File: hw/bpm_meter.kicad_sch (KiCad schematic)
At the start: 72 parts, among them J1 Conn_01x03_Pin, Q1 AO3400A, Q10 DMN2004VK, Q11 DMN2004VK, Q12 DMN2004VK, Q13 DMN2004VK, Q2 DMN2004VK, Q3 DMN2004VK, Q4 DMN2004VK, Q5 DMN2004VK, Q6 DMN2004VK, Q7 DMN2004VK, Q8 DMN2004VK, Q9 DMN2004VK, U1 SLS0391FR1A1GD, U2 AOZ1282CI, U3 H11L1, U4 SLS0391FR1A1GD, U5 SLS0391FR1A1GD

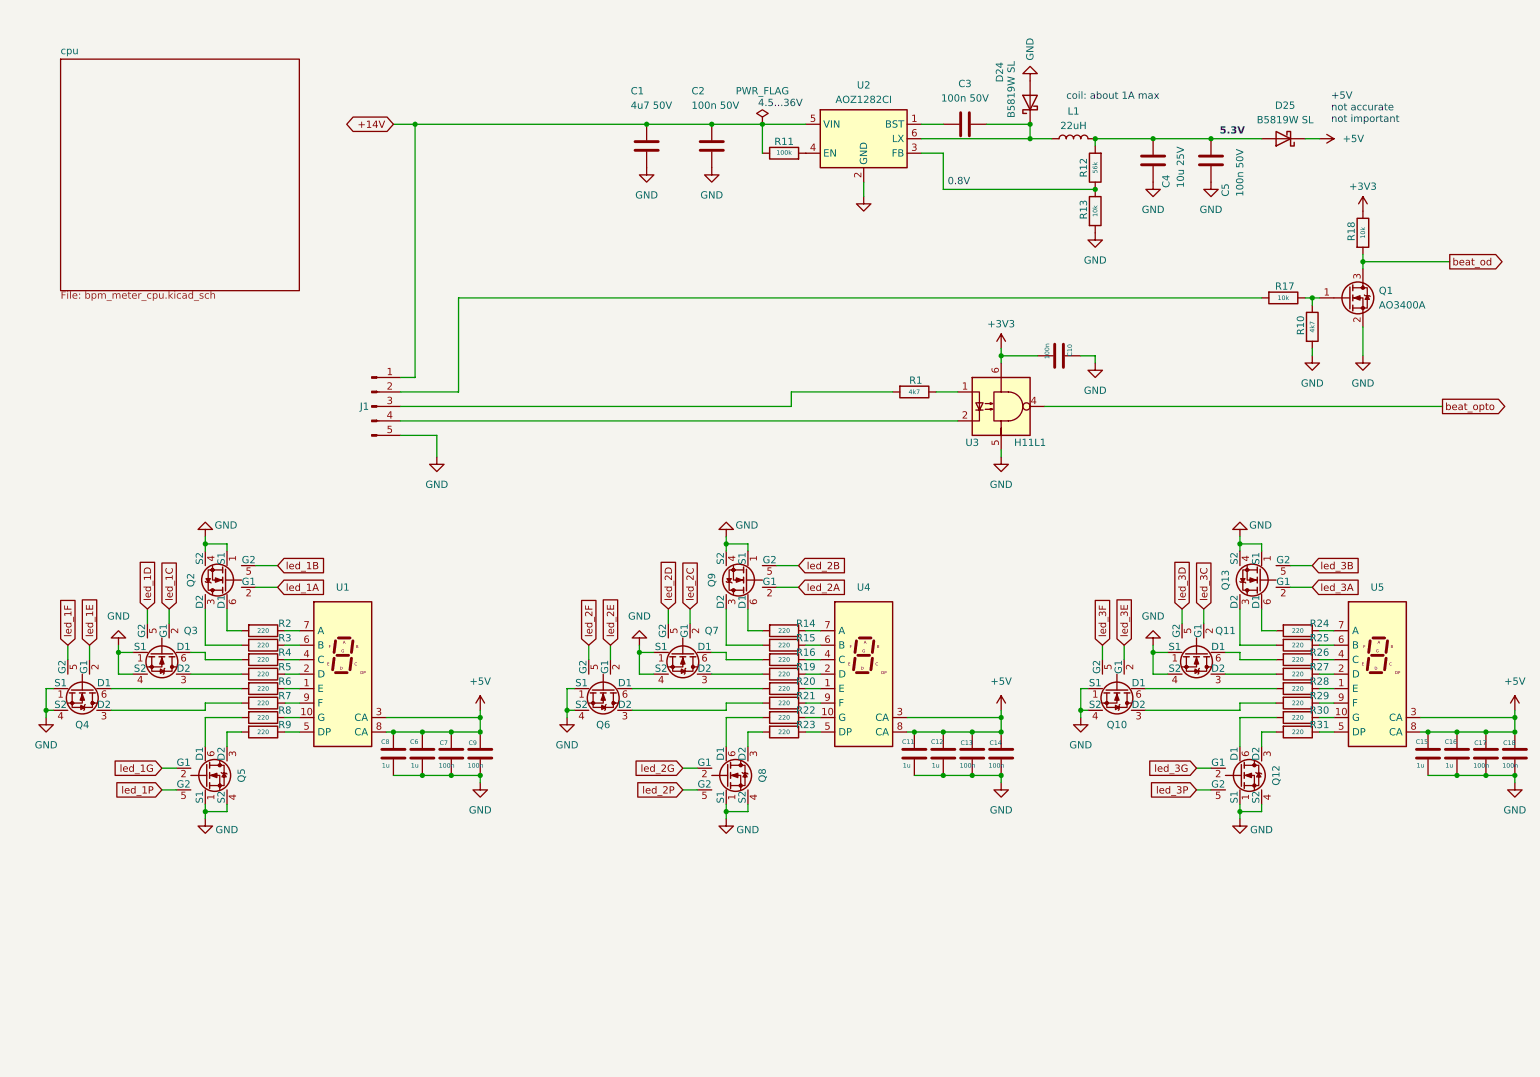
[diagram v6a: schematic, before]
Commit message: Now using LP5030 LED driver
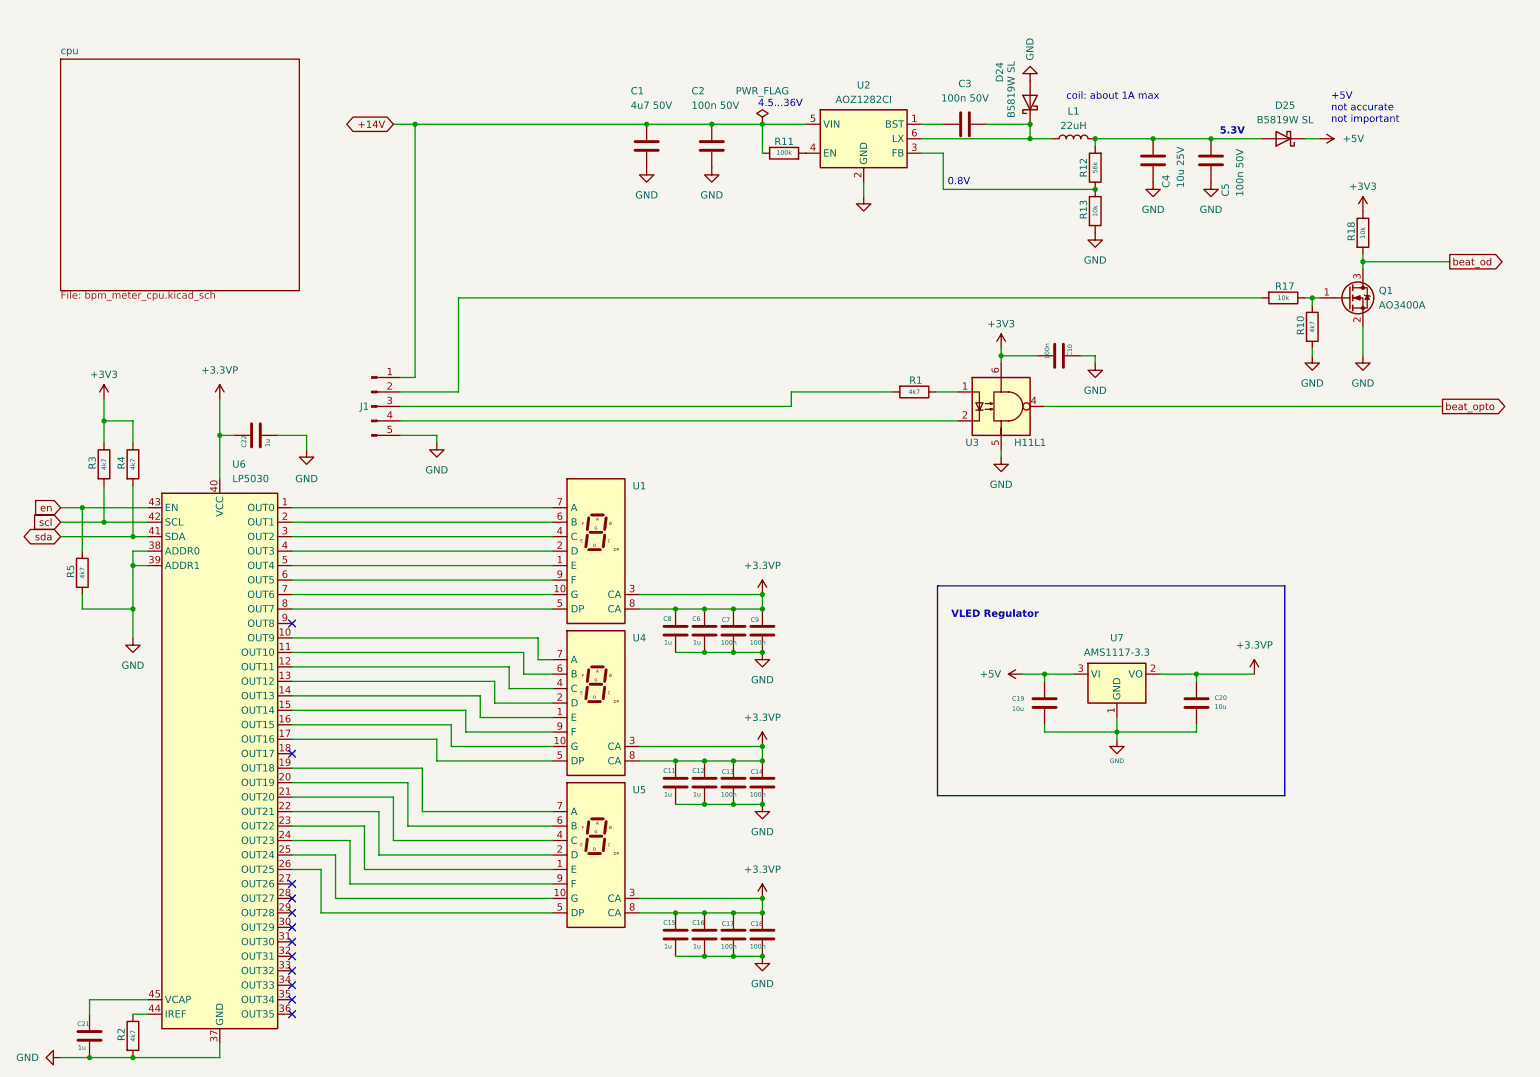
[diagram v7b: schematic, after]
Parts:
- removed Q10, Q11, Q12, Q13, Q2, Q3, Q4, Q5, Q6, Q7, Q8, Q9: DMN2004VK, Package_TO_SOT_SMD:SOT-563, symbol 00_project_library:DMN60H080DS
- removed R14, R15, R16, R19, R20, R21, R22, R23, R24, R25, R26, R27, R28, R29, R30, R31, R6, R7, R8, R9: 220, Resistor_SMD:R_0402_1005Metric_Pad0.72x0.64mm_HandSolder, symbol Device:R
- added C19, C20: 10u, Capacitor_SMD:C_0603_1608Metric, symbol 00_project_library:C
- added C21, C22: 1u, Capacitor_SMD:C_0402_1005Metric, symbol 00_project_library:C
- added U6: LP5030, Package_DFN_QFN:VQFN-46-1EP_5x6mm_P0.4mm_EP2.8x3.8mm, symbol Driver_LED:LP5036
- added U7: AMS1117-3.3, 00_project_library:SOT-223-3_TabPin2, symbol 00_project_library:AMS1117-3.3
- J1: value Conn_01x03_Pin -> Conn_01x05_Pin
- R2, R3, R4, R5: value 220 -> 4k7; JLC C25091 -> (none)
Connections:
- net +3V3: now also R3.1, R4.1
- net +5V: now also C19.1, U7.3 (VI); no longer C11.1, C12.1, C13.1, C14.1, C15.1, C16.1, C17.1, C18.1, C6.1, C7.1, C8.1, C9.1, U1.3 (CA), U1.8 (CA), U4.3 (CA), U4.8 (CA), U5.3 (CA), U5.8 (CA)
- net GND: now also R2.2, R5.2, C19.2, C20.2, C21.2, C22.2, U6.37 (GND), U6.38 (ADDR0), U6.39 (ADDR1), U6.46 (GND), U6.47 (GND), U7.1 (GND)
- net scl: now reaches R3.2
- net scl: now also U6.42 (SCL)
- net at U1.7 (A): now also U6.1 (OUT0); no longer R2.1
- net at U4.4 (C): now also U6.12 (OUT11)
- net at U4.9 (F): now also U6.15 (OUT14)
- net at U1.9 (F): now also U6.6 (OUT5)
- net at U5.7 (A): now also U6.19 (OUT18)
- net at U5.10 (G): now also U6.25 (OUT24)
- net at U5.1 (E): now also U6.23 (OUT22)
- net at U5.2 (D): now also U6.22 (OUT21)
- net at U5.4 (C): now also U6.21 (OUT20)
- net at U5.5 (DP): now also U6.26 (OUT25)
- net at U5.6 (B): now also U6.20 (OUT19)
- net at U5.9 (F): now also U6.24 (OUT23)
- net at U1.4 (C): now also U6.3 (OUT2); no longer R4.1
- net sda: now reaches R4.2
- net sda: now also U6.41 (SDA)
- net at U4.7 (A): now also U6.10 (OUT9)
- net at U1.1 (E): now also U6.5 (OUT4)
- net at U1.10 (G): now also U6.7 (OUT6)
- net at U1.2 (D): now also U6.4 (OUT3); no longer R5.1
- net at U1.5 (DP): now also U6.8 (OUT7)
- net at U1.6 (B): now also U6.2 (OUT1); no longer R3.1
- net at U4.2 (D): now also U6.13 (OUT12)
- net at U4.1 (E): now also U6.14 (OUT13)
- net at U4.6 (B): now also U6.11 (OUT10)
- net at U4.10 (G): now also U6.16 (OUT15)
- net at U4.5 (DP): now also U6.17 (OUT16)
- new net: R2.1, U6.44 (IREF)
- new net: C21.1, U6.45 (VCAP)
- new net +3.3VP: C11.1, C12.1, C13.1, C14.1, C15.1, C16.1, C17.1, C18.1, C20.1, C22.1, C6.1, C7.1, C8.1, C9.1, U1.3 (CA), U1.8 (CA), U4.3 (CA), U4.8 (CA), U5.3 (CA), U5.8 (CA), U6.40 (VCC), U7.2 (VO)
- new net en: R5.1, U6.43 (EN)
- no-connect marks 0 -> 12
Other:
- note added: "VLED Regulator"
- moved on the sheet: C11, C12, C13, C14, C15, C16, C17, C18, C6, C7, C8, C9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

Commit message: Changed LED driver to ISSI IS31FL3236A
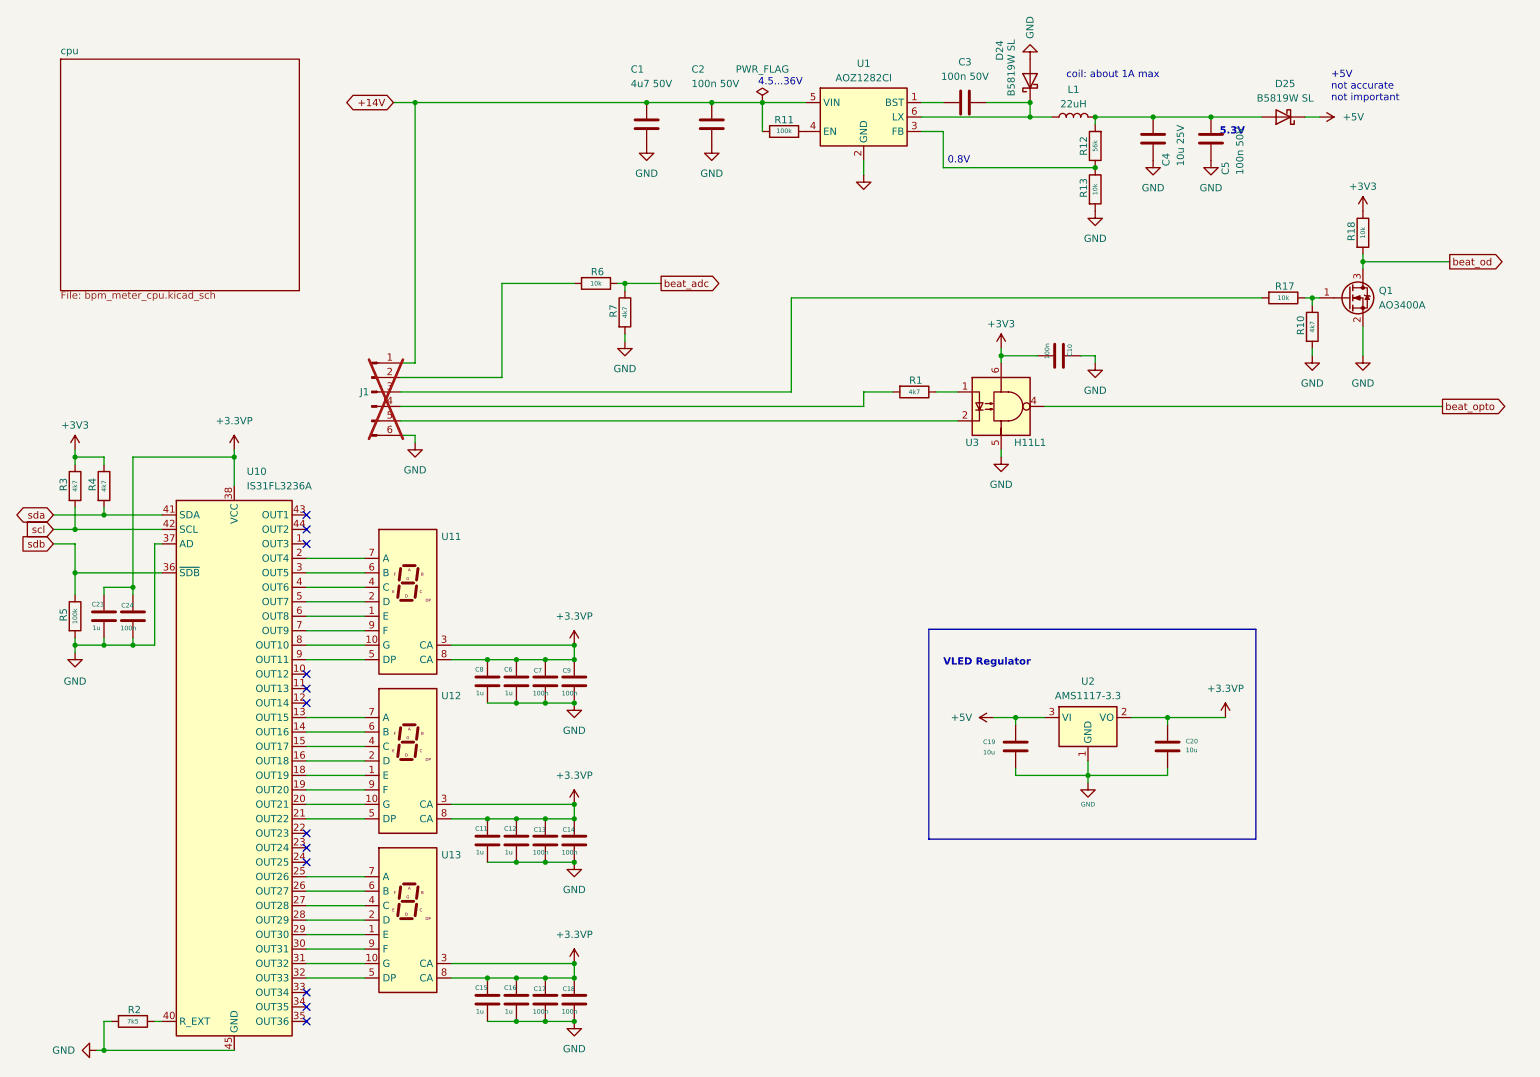
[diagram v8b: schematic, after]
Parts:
- removed C21, C22: 1u, Capacitor_SMD:C_0402_1005Metric, symbol 00_project_library:C
- removed U6: LP5030, Package_DFN_QFN:VQFN-46-1EP_5x6mm_P0.4mm_EP2.8x3.8mm, symbol Driver_LED:LP5036
- added C23: 1u, Capacitor_SMD:C_0402_1005Metric_Pad0.74x0.62mm_HandSolder, symbol 00_project_library:C
- added C24: 100n, Capacitor_SMD:C_0402_1005Metric_Pad0.74x0.62mm_HandSolder, symbol 00_project_library:C
- added R6: 10k, Resistor_SMD:R_0402_1005Metric_Pad0.72x0.64mm_HandSolder, symbol Device:R
- added R7: 4k7, Resistor_SMD:R_0402_1005Metric_Pad0.72x0.64mm_HandSolder, symbol Device:R
- added U10: IS31FL3236A, 00_project_library:QFN-44-5x5mm_P0.4mm, symbol 00_project_library:IS31FL3236A
- C10, C13, C14, C17, C18, C7, C9: footprint Capacitor_SMD:C_0402_1005Metric -> Capacitor_SMD:C_0402_1005Metric_Pad0.74x0.62mm_HandSolder; JLC C307331 -> (none)
- C11, C12, C15, C16, C6, C8: footprint Capacitor_SMD:C_0402_1005Metric -> Capacitor_SMD:C_0402_1005Metric_Pad0.74x0.62mm_HandSolder; JLC C52923 -> (none)
- J1: value Conn_01x05_Pin -> Conn_01x06_Pin; footprint Connector_PinHeader_2.54mm:PinHeader_1x05_P2.54mm_Vertical -> Connector_PinHeader_2.54mm:PinHeader_1x06_P2.54mm_Vertical; symbol Connector:Conn_01x05_Pin -> Connector:Conn_01x06_Pin; now not fitted
- R2: value 4k7 -> 7k5
- R5: value 4k7 -> 100k
- renumbered U2 to U1, U1 to U11, U4 to U12, U5 to U13, U7 to U2
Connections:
- net +3.3VP: now also C23.1, C24.1, U10.38 (VCC)
- net GND: now also J1.6 (Pin_6), C23.2, C24.2, R7.2, U10.17 (GND), U10.37 (AD), U10.39 (GND), U10.45 (GND); no longer J1.5 (Pin_5)
- net scl: now also U10.42 (SCL)
- net sda: now also U10.41 (SDA)
- net at U11.7 (A): now also U10.2 (OUT4)
- net at U12.7 (A): now also U10.13 (OUT15)
- net at U12.6 (B): now also U10.14 (OUT16)
- net at U12.4 (C): now also U10.15 (OUT17)
- net at U12.2 (D): now also U10.16 (OUT18)
- net at U12.1 (E): now also U10.18 (OUT19)
- net at U12.9 (F): now also U10.19 (OUT20)
- net at U12.10 (G): now also U10.20 (OUT21)
- net at U12.5 (DP): now also U10.21 (OUT22)
- net at U13.7 (A): now also U10.25 (OUT26)
- net at U11.6 (B): now also U10.3 (OUT5)
- net at U13.6 (B): now also U10.26 (OUT27)
- net at U13.4 (C): now also U10.27 (OUT28)
- net at U13.2 (D): now also U10.28 (OUT29)
- net at U13.1 (E): now also U10.29 (OUT30)
- net at U13.9 (F): now also U10.30 (OUT31)
- net at U13.10 (G): now also U10.31 (OUT32)
- net at U13.5 (DP): now also U10.32 (OUT33)
- net at U11.4 (C): now also U10.4 (OUT6)
- net at U11.2 (D): now also U10.5 (OUT7)
- net at R2.1: now also U10.40 (R_EXT)
- net at U11.1 (E): now also U10.6 (OUT8)
- net at U11.9 (F): now also U10.7 (OUT9)
- net at U11.10 (G): now also U10.8 (OUT10)
- net at U11.5 (DP): now also U10.9 (OUT11)
- net at R17.2: now also J1.3 (Pin_3); no longer J1.2 (Pin_2)
- net at U3.2: now also J1.5 (Pin_5); no longer J1.4 (Pin_4)
- net at R1.2: now also J1.4 (Pin_4); no longer J1.3 (Pin_3)
- net en renamed sdb
- net sdb: now also U10.36 (~{SDB})
- new net: J1.2 (Pin_2), R6.2
- new net beat_adc: R6.1, R7.1
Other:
- moved on the sheet: C1, C11, C12, C13, C14, C15, C16, C17, C18, C19, C2, C20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
